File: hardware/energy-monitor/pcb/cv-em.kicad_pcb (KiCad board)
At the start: 2 copper layers, 88.8 x 74.5 mm, 32 parts, among them J3 3.5mm jack, U1 ESP32-WROOM-32E (4MB), U2 AMS1117-3.3

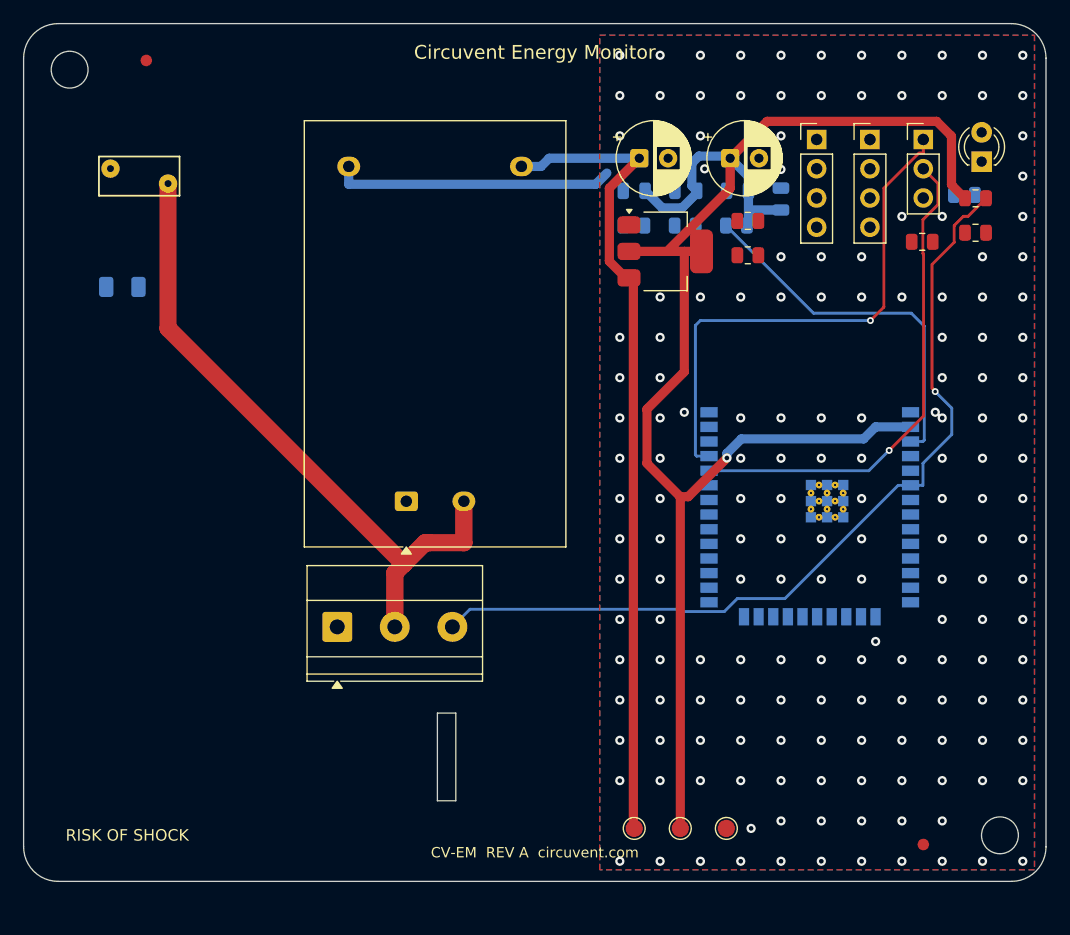
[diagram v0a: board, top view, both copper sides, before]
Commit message: hardware: fix mains isolation barrier gaps, add load-controller PCB
Adds the 13th board (ultra-compact dual-channel load controller: ESP32-C3,
opto+relay channel, MOSFET PWM channel, USB-C, AP2112K LDO, USBLC6 ESD) and
regenerates all 12 existing boards, which were stale with respect to earlier
relay-pinout and LED-polarity fixes.

The substantive change is to the mains isolation barrier. It is a keepout band
the router must not cross, deliberately cut where a component straddles it
because there the isolation is provided by the part's package. Three linked
defects made those cuts unsafe, each only visible once the previous was fixed:

1. The cut removed the barrier across the full band width for the straddling
   part's whole height, while the ISO_BRIDGE area that excuses the gap covered
   only the part itself. The router used the leftover strip beside the part to
   bring +5V within 6.99 mm of AC_N against an 8.0 mm reinforced creepage rule.
2. Straddling parts can overlap in y, so cutting per part put one part's
   keepout on another part's pads. The exempt x-ranges are now unioned per
   strip by a sweep line.
3. The rule only relaxes for items insideArea('ISO_BRIDGE'). With the hole the
   same size as the area, a track could hug the hole's edge without being
   contained in it, so the rule fired anyway and the router had no way to know.
   The hole is now the part's pad bbox + 0.3 mm, strictly inside ISO_BRIDGE at
   the footprint bbox + 0.6 mm.

The tighter hole leaves mains nets less room to reach bridge pads, so some
boards report more unconnected items. That is deliberate: those are documented
hand-routing items, whereas a creepage violation is a safety defect.

Also fixed in the generator:
- _pad_shape() derived a pad's layers from PAD::GetLayer(), which returns F.Cu
  even for pads on B.Cu. Every back-side pad became a phantom obstacle on the
  front, blocking legal paths there while hiding the real one behind. Only
  IsOnLayer() is truthful.
- Castella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
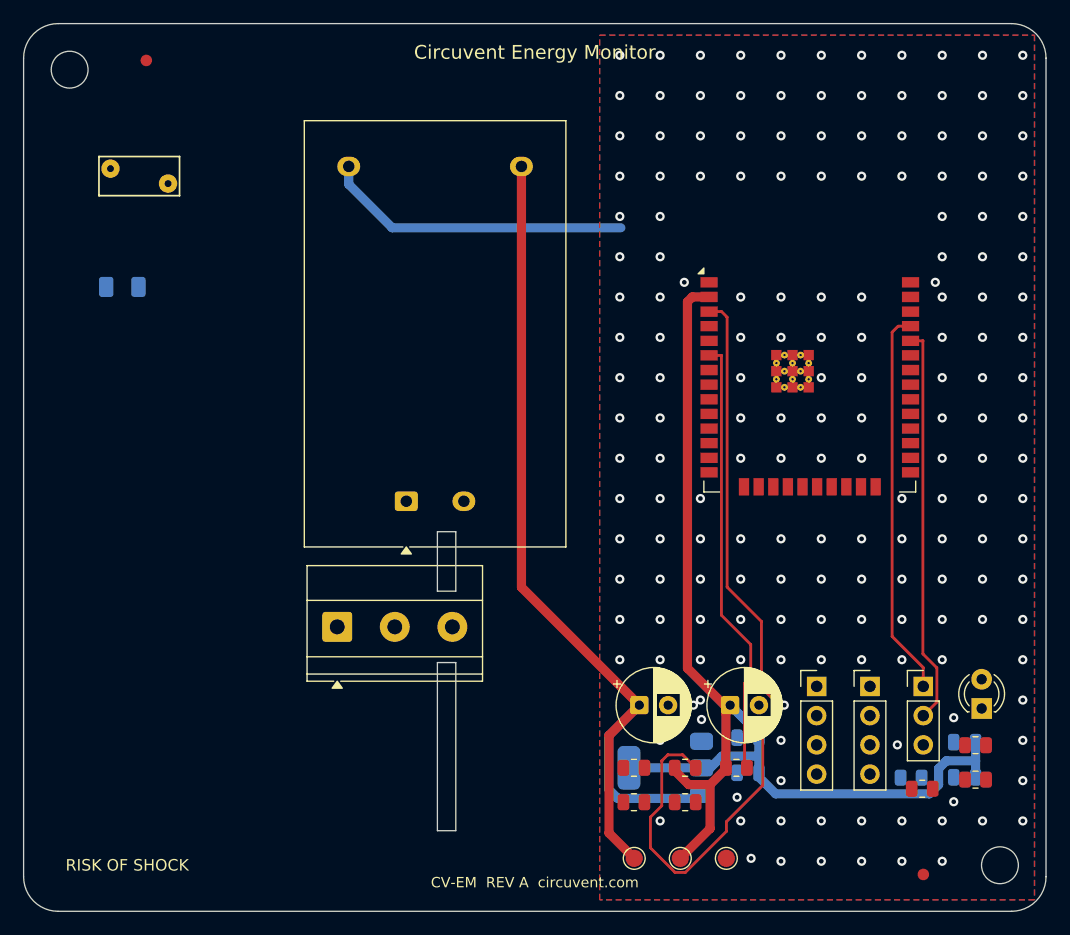
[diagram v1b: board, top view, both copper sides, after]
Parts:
- R1, Rbias1, Rbias2, U1: moved to F.Cu
- U2: moved to B.Cu
- moved R5 54.7 mm to (153.0, 147.6)
- moved Rbias1 54.0 mm to (182.7, 142.7), turned to 0 degrees
- moved C3 53.7 mm to (181.7, 142.4)
- moved R2 53.6 mm to (161.9, 144.6)
- moved C5 52.7 mm to (181.7, 145.5), turned to 180 degrees
- moved R3 52.4 mm to (182.7, 145.7)
- moved Rb 50.8 mm to (177.1, 145.5)
- moved C4 50.6 mm to (162.9, 145.1)
- moved Cb 48.5 mm to (162.9, 142.0)
- moved R4 48.5 mm to (178.0, 146.5)
- moved R6 47.8 mm to (157.5, 147.6)
- moved LED0 47.5 mm to (183.2, 139.5)
- moved C1 47.5 mm to (153.5, 139.2)
- moved C2 47.5 mm to (161.4, 139.2)
- moved CT1 47.5 mm to (168.9, 137.6)
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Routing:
- net AC_N: track 56.9 -> 0.00 mm
- net +3V3: track 140.5 -> 101.2 mm, vias 1 -> 0
- net EN: track 32.0 -> 70.3 mm
- net CT_PIN: track 75.0 -> 38.2 mm, vias 1 -> 0
- net +5V: track 70.9 -> 83.3 mm
- net UART_TX: track 45.7 -> 33.7 mm, vias 1 -> 0
- net UART_RX: track 43.2 -> 34.6 mm, vias 1 -> 0
- net GND: track 24.4 -> 26.8 mm, vias 171 -> 179
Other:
- board size 88.8 x 74.5 mm -> 88.8 x 77.1 mm

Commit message: Release 1.10.0, and stop shipping permissions the app never uses
Cut 1.10.0 (versionCode 12) and built it: AAB 38 MB, APK 83 MB, signed with the
upload key, JS bundle embedded.

Checking the generated manifest before writing the Play listing turned up
permissions no one had asked for. Every one of them is printed on the store page
for users to read before they install:

  RECORD_AUDIO          expo-camera asks for the microphone so video can be
                        recorded with sound. This app only ever puts the camera
                        in barcode mode to read a QR label, and expo-speech is
                        output-only - it speaks, it does not listen. Left in,
                        Play lists "Microphone" against a home-control app,
                        which is alarming, unexplainable and untrue.
  SYSTEM_ALERT_WINDOW   React Native's development overlay, useless in a release
                        build and shown to users as "Display over other apps".
  READ/WRITE_EXTERNAL_STORAGE
                        Legacy storage access nothing here touches.

Stripped via android.blockedPermissions. That emits tools:node="remove", which
is a merge instruction rather than a guarantee, so it was checked against the
finished artifact with aapt2 rather than the source manifest - all four are
absent from the APK.

NEARBY_WIFI_DEVICES now carries neverForLocation. Android otherwise treats it as
location-capable, because knowing which networks are in range is enough to place
someone, and Play's data safety review treats it the same way. The app uses it
only to join a new device's setup hotspot. That flag is a promise, so the plugin
says plainly that it has to come off if scan results are ever used positionally.

What is left is defensible: location for Wi-Fi onboarding (Android requires it),
camera for the QR label, nearby-devices flagged as non-positional.

Added mobile/store/listing with the text Play asks for - title, short and full
descriptions, and what'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
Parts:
- moved J3 32.0 mm to (112.0, 104.3), turned to 90 degrees
- moved RV1 23.1 mm to (107.5, 115.7)
- moved F1 23.1 mm to (108.6, 126.0)
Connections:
- J3 pad 3: CT_PIN -> PE
- LED0 pad 1: N$LED0.1 -> GND
- LED0 pad 2: N$LED0.2 -> LED0_A
- R2 pad 2: CT_PIN -> LED0_A
- R3 pad 1: N$R3.1 -> +3V3
- R3 pad 2: N$R3.2 -> CT_PIN
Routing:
- net EN: track 70.3 -> 41.6 mm
- net LED0_A: track 0.00 -> 24.8 mm
- net CT_PIN: track 38.2 -> 61.0 mm, vias 0 -> 2
- net AC_N: track 0.00 -> 22.1 mm
- net +3V3: track 101.2 -> 114.3 mm, vias 0 -> 1
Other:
- outline, holes or cut-outs redrawn
- board text added: "!! MAINS !!"
